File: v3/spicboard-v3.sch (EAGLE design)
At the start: 39 parts, among them IC1 74HC595N, Q1 BC557, Q2 BC557

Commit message: Schieberegister mit Pull-Up-Widerstand
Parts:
- added R15: 1k, resistor:R-EU_0207/10
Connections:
- net GND: no longer IC1A.G
- net SS: now also IC1A.G, R15.1
- net VCC: now also R15.2
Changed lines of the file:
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@@
 <part name="R9" library="resistor" deviceset="R-EU_" device="0207/10" value="1k"/>
 <part name="R11" library="resistor" deviceset="R-EU_" device="0207/10" value="1k"/>
-<part name="GND5" library="supply1" deviceset="GND" device=""/>
 <part name="P+7" library="supply1" deviceset="VCC" device=""/>
 <part name="C1" library="capacitor-wima" deviceset="C" device="2.5/2" value="100n"/>
@@
 <part name="EXT" library="SparkFun-Connectors" deviceset="CONN_04" device=""/>
 <part name="COM" library="SparkFun-Connectors" deviceset="CONN_03" device=""/>
+<part name="R15" library="resistor" deviceset="R-EU_" device="0207/10" value="1k"/>
+<part name="P+9" library="supply1" deviceset="VCC" device=""/>
 </parts>
 <sheets>
@@
 <instance part="R9" gate="G$1" x="137.16" y="101.6" rot="R270"/>
 <instance part="R11" gate="G$1" x="106.68" y="96.52"/>
-<instance part="GND5" gate="1" x="93.98" y="12.7"/>
 <instance part="P+7" gate="VCC" x="93.98" y="55.88"/>
 <instance part="C1" gate="G$1" x="172.72" y="30.48"/>
@@
 <instance part="EXT" gate="G$1" x="43.18" y="-17.78" rot="R180"/>
 <instance part="COM" gate="J$1" x="81.28" y="-17.78" rot="R180"/>
+<instance part="R15" gate="G$1" x="99.06" y="15.24"/>
+<instance part="P+9" gate="VCC" x="111.76" y="20.32"/>
 </instances>
 <busses>
@@
 <pinref part="P+7" gate="VCC" pin="VCC"/>
 </segment>
+<segment>
+<pinref part="R15" gate="G$1" pin="2"/>
+<pinref part="P+9" gate="VCC" pin="VCC"/>
+<wire x1="104.14" y1="15.24" x2="111.76" y2="15.24" width="0.1524" layer="91"/>
+<wire x1="111.76" y1="15.24" x2="111.76" y2="17.78" width="0.1524" layer="91"/>
+</segment>
 </net>
 <net name="GND" class="0">
@@
 <pinref part="R9" gate="G$1" pin="1"/>
 <pinref part="GND4" gate="1" pin="GND"/>
-</segment>
-<segment>
-<pinref part="IC1" gate="A" pin="G"/>
-<pinref part="GND5" gate="1" pin="GND"/>
-<wire x1="96.52" y1="27.94" x2="93.98" y2="27.94" width="0.1524" layer="91"/>
-<wire x1="93.98" y1="27.94" x2="93.98" y2="15.24" width="0.1524" layer="91"/>
 </segment>
 <segment>
@@
 <pinref part="B1" gate="G$1" pin="*D10"/>
 <pinref part="IC1" gate="A" pin="RCK"/>
-<wire x1="76.2" y1="38.1" x2="96.52" y2="38.1" width="0.1524" layer="91"/>
+<wire x1="76.2" y1="38.1" x2="93.98" y2="38.1" width="0.1524" layer="91"/>
 <label x="78.74" y="38.1" size="1.778" layer="95"/>
-</segment>
-</net>
+<pinref part="IC1" gate="A" pin="G"/>
+<wire x1="93.98" y1="38.1" x2="96.52" y2="38.1" width="0.1524" layer="91"/>
+<wire x1="96.52" y1="27.94" x2="93.98" y2="27.94" width="0.1524" layer="91"/>
+<wire x1="93.98" y1="27.94" x2="93.98" y2="38.1" width="0.1524" layer="91"/>
+<junction x="93.98" y="38.1"/>
+<pinref part="R15" gate="G$1" pin="1"/>
+<wire x1="93.98" y1="15.24" x2="93.98" y2="27.94" width="0.1524" layer="91"/>
+<junction x="93.98" y="27.94"/>
+</segment>
+</net>

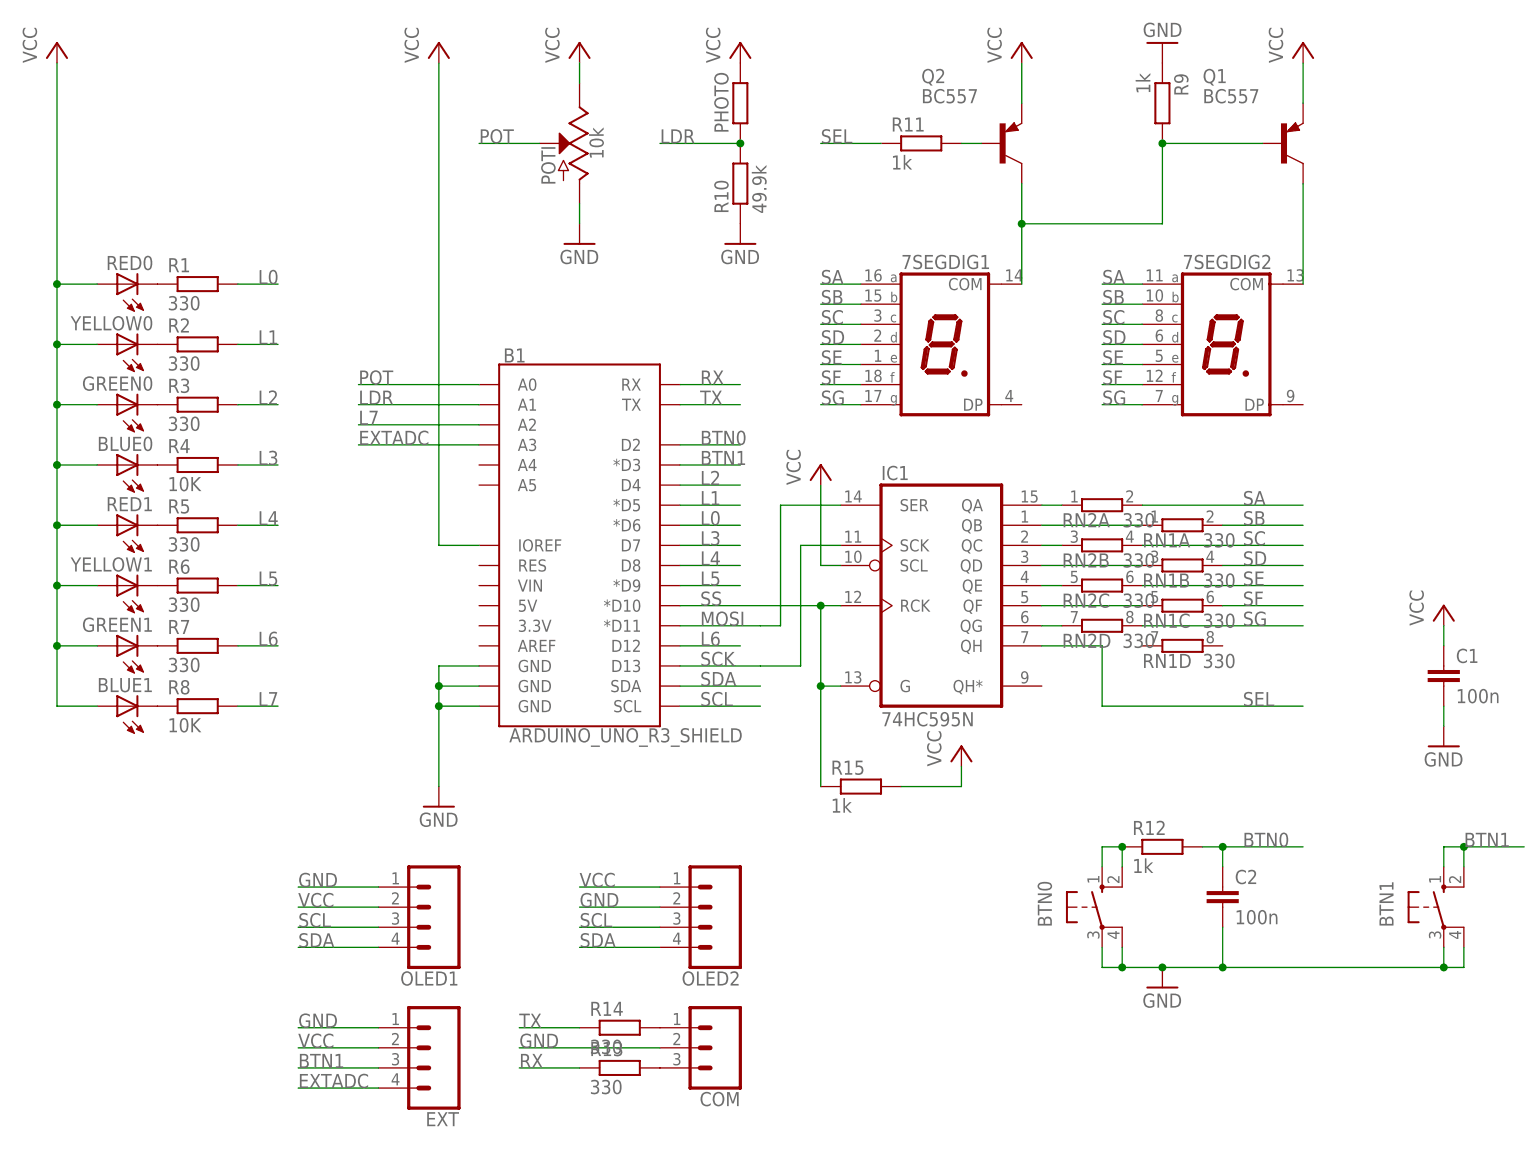
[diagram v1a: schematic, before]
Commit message: Beschriftungen (Layer)
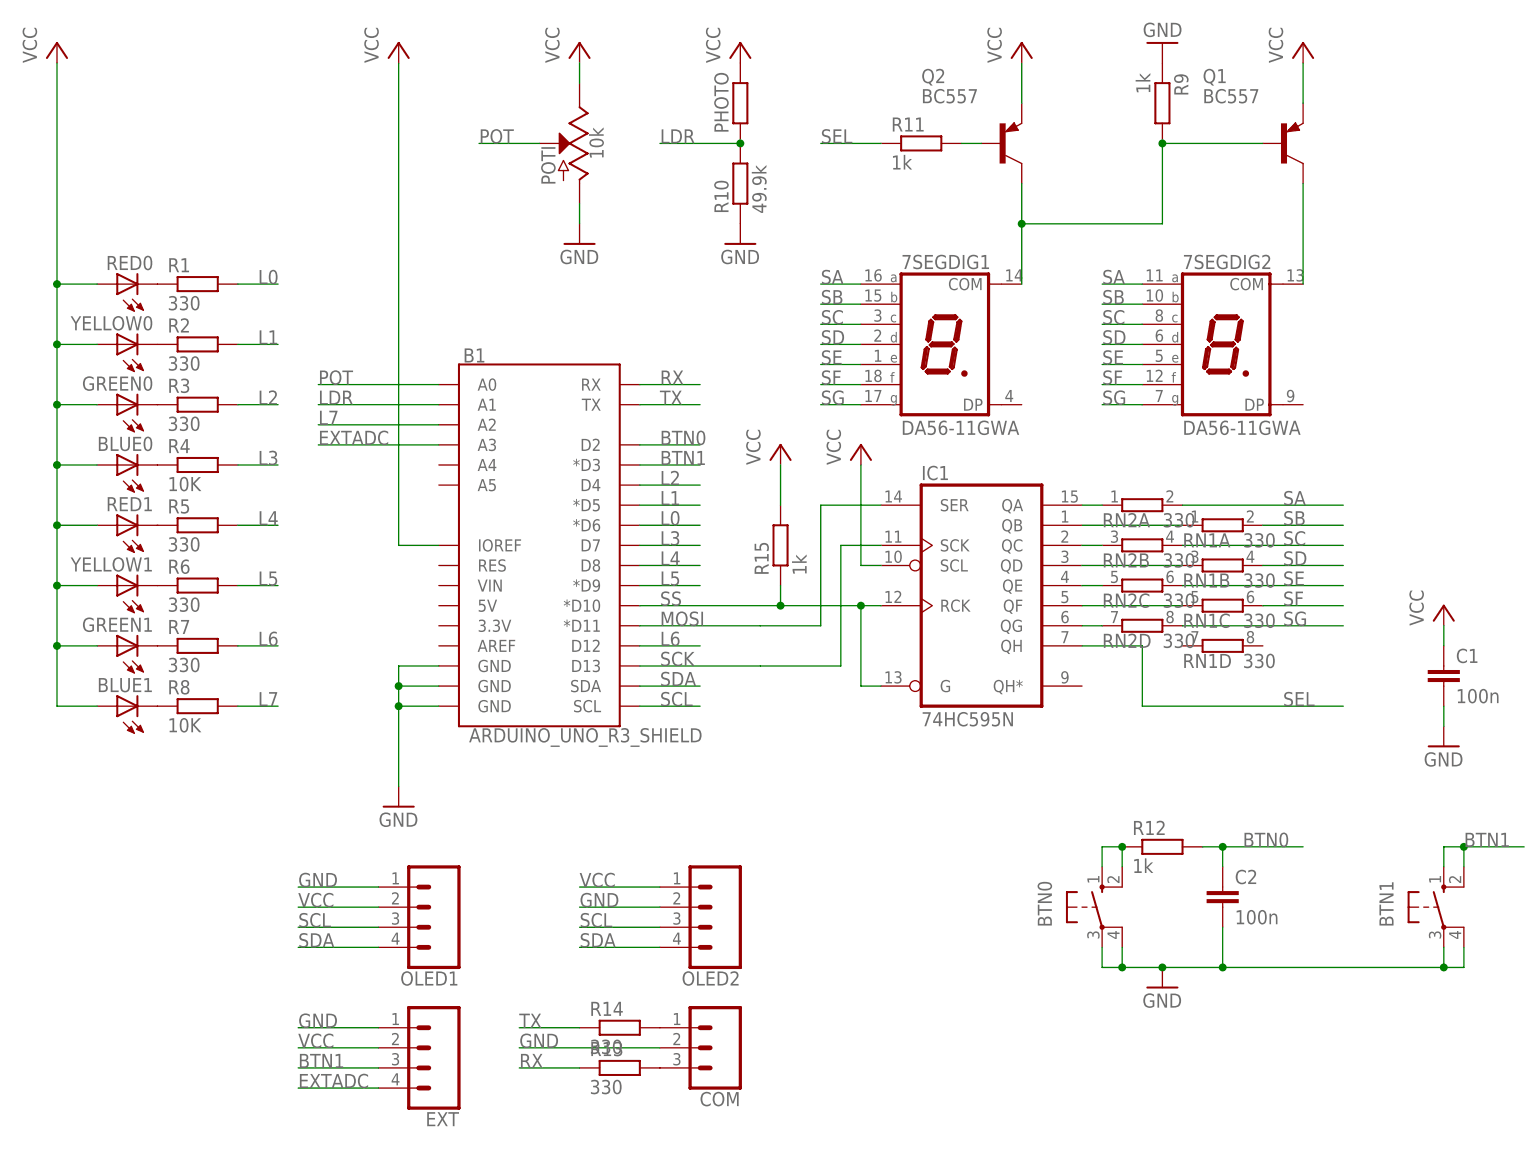
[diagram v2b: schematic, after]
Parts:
- PHOTO: value LDRLDR -> LDR; device spicboard-v3:LDRLDR -> spicboard-v3:LDR
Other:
- moved on the sheet: B1, IC1, R15, RN1A, RN1B, RN1C, RN1D, RN2A, RN2B, RN2C, RN2D

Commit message: Beschriftungen (nochmal)
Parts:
- IC1: value 74HC595N -> 74HC595
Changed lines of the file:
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@@
 <part name="R7" library="resistor" deviceset="R-EU_" device="0207/10" value="330"/>
 <part name="R8" library="resistor" deviceset="R-EU_" device="0207/10" value="10K"/>
-<part name="IC1" library="74xx-eu" deviceset="74*595" device="N" technology="HC"/>
+<part name="IC1" library="74xx-eu" deviceset="74*595" device="N" technology="HC" value="74HC595"/>
 <part name="PHOTO" library="spicboard-v3" deviceset="LDR" device="" value="LDR"/>
 <part name="POTI" library="spicboard-v3" deviceset="POTENTIOMETER" device="-PTH-9MM-1/20W-20%" value="10k"/>

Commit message: IOREF nach VCC umbenannt
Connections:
- net VCC: now also B1.VCC; no longer B1.IOREF
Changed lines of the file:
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@@
 <wire x1="40.64" y1="45.72" x2="40.64" y2="106.68" width="0.1524" layer="91"/>
 <pinref part="P+3" gate="VCC" pin="VCC"/>
-<pinref part="B1" gate="G$1" pin="IOREF"/>
+<pinref part="B1" gate="G$1" pin="VCC"/>
 <wire x1="40.64" y1="45.72" x2="45.72" y2="45.72" width="0.1524" layer="91"/>
 </segment>

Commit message: SPiCboard: 10K -> 10k
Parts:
- R4, R8: value 10K -> 10k
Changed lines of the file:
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@@
 <part name="R2" library="resistor" deviceset="R-EU_" device="0207/10" value="330"/>
 <part name="R3" library="resistor" deviceset="R-EU_" device="0207/10" value="330"/>
-<part name="R4" library="resistor" deviceset="R-EU_" device="0207/10" value="10K"/>
+<part name="R4" library="resistor" deviceset="R-EU_" device="0207/10" value="10k"/>
 <part name="R5" library="resistor" deviceset="R-EU_" device="0207/10" value="330"/>
 <part name="R6" library="resistor" deviceset="R-EU_" device="0207/10" value="330"/>
 <part name="R7" library="resistor" deviceset="R-EU_" device="0207/10" value="330"/>
-<part name="R8" library="resistor" deviceset="R-EU_" device="0207/10" value="10K"/>
+<part name="R8" library="resistor" deviceset="R-EU_" device="0207/10" value="10k"/>
 <part name="IC1" library="74xx-eu" deviceset="74*595" device="N" technology="HC" value="74HC595"/>
 <part name="PHOTO" library="spicboard-v3" deviceset="LDR" device="" value="LDR"/>
